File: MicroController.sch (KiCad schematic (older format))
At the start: 59 parts, among them J301 Conn_02x03_Odd_Even, Q301 IRLML0040TR, Q302 IRLML0040TR, SW301 TACTILE_SWITCHPTS540-SMD, SW302 TACTILE_SWITCHPTS540-SMD, SW303 TACTILE_SWITCHPTS540-SMD, SW304 TACTILE_SWITCHPTS540-SMD, SW305 TACTILE_SWITCHPTS540-SMD, SW306 TACTILE_SWITCHPTS540-SMD, SW307 TACTILE_SWITCHPTS540-SMD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

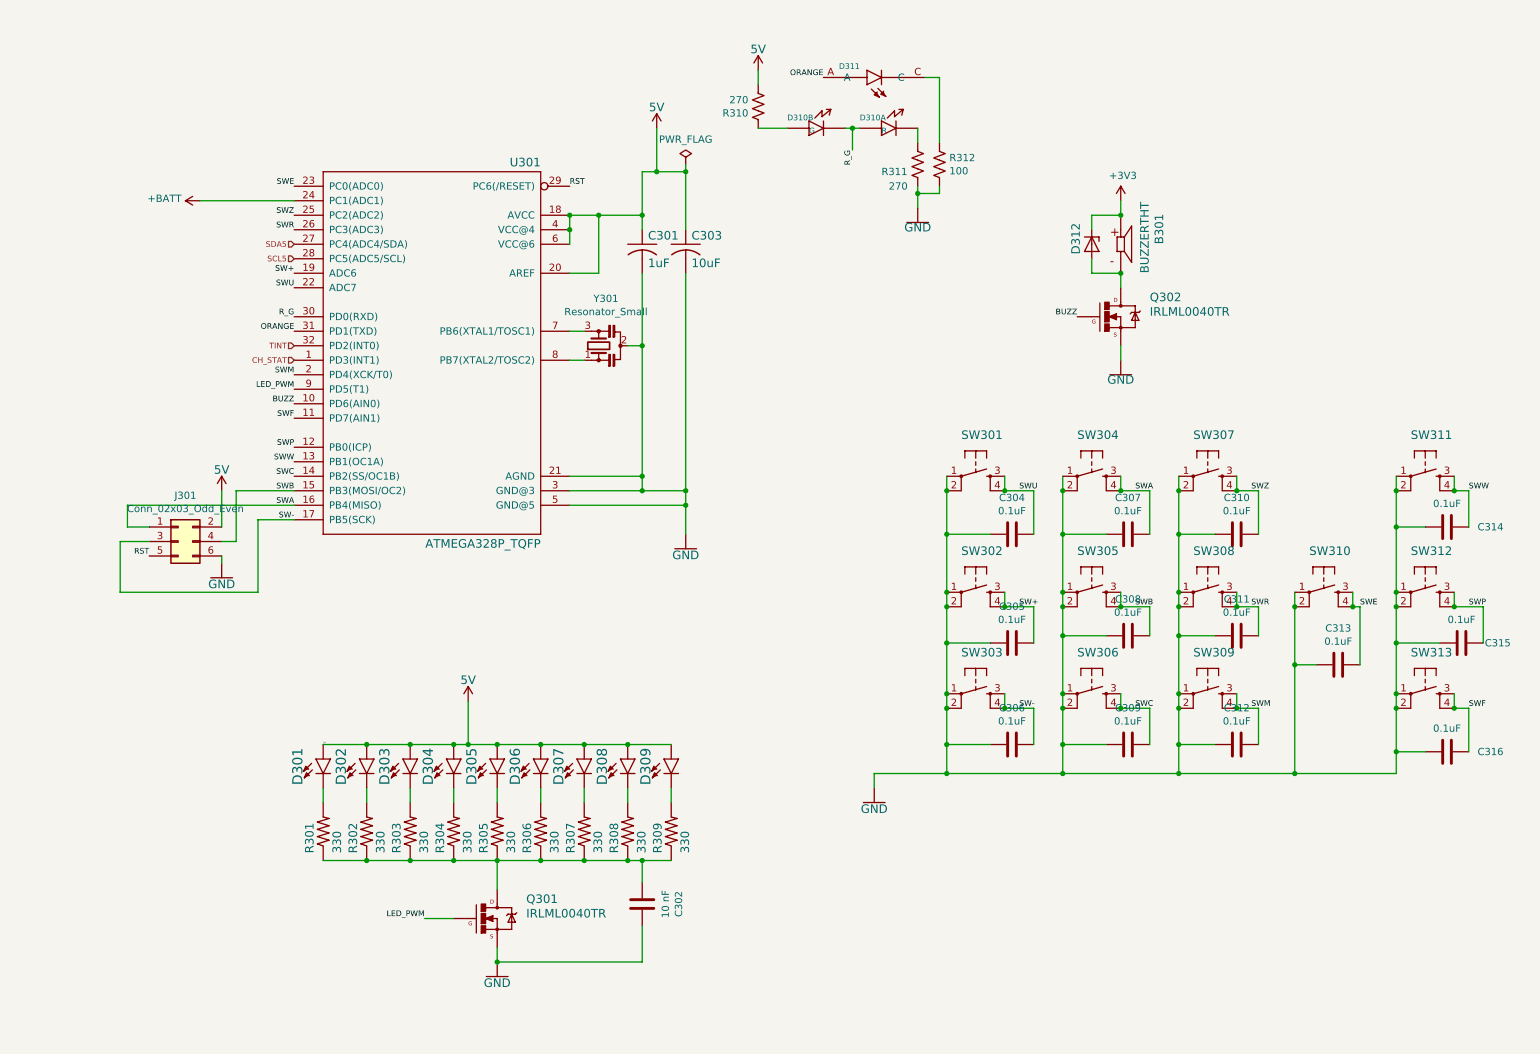
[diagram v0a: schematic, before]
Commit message: Last version before switching to resistive model to read the scroll wheel.
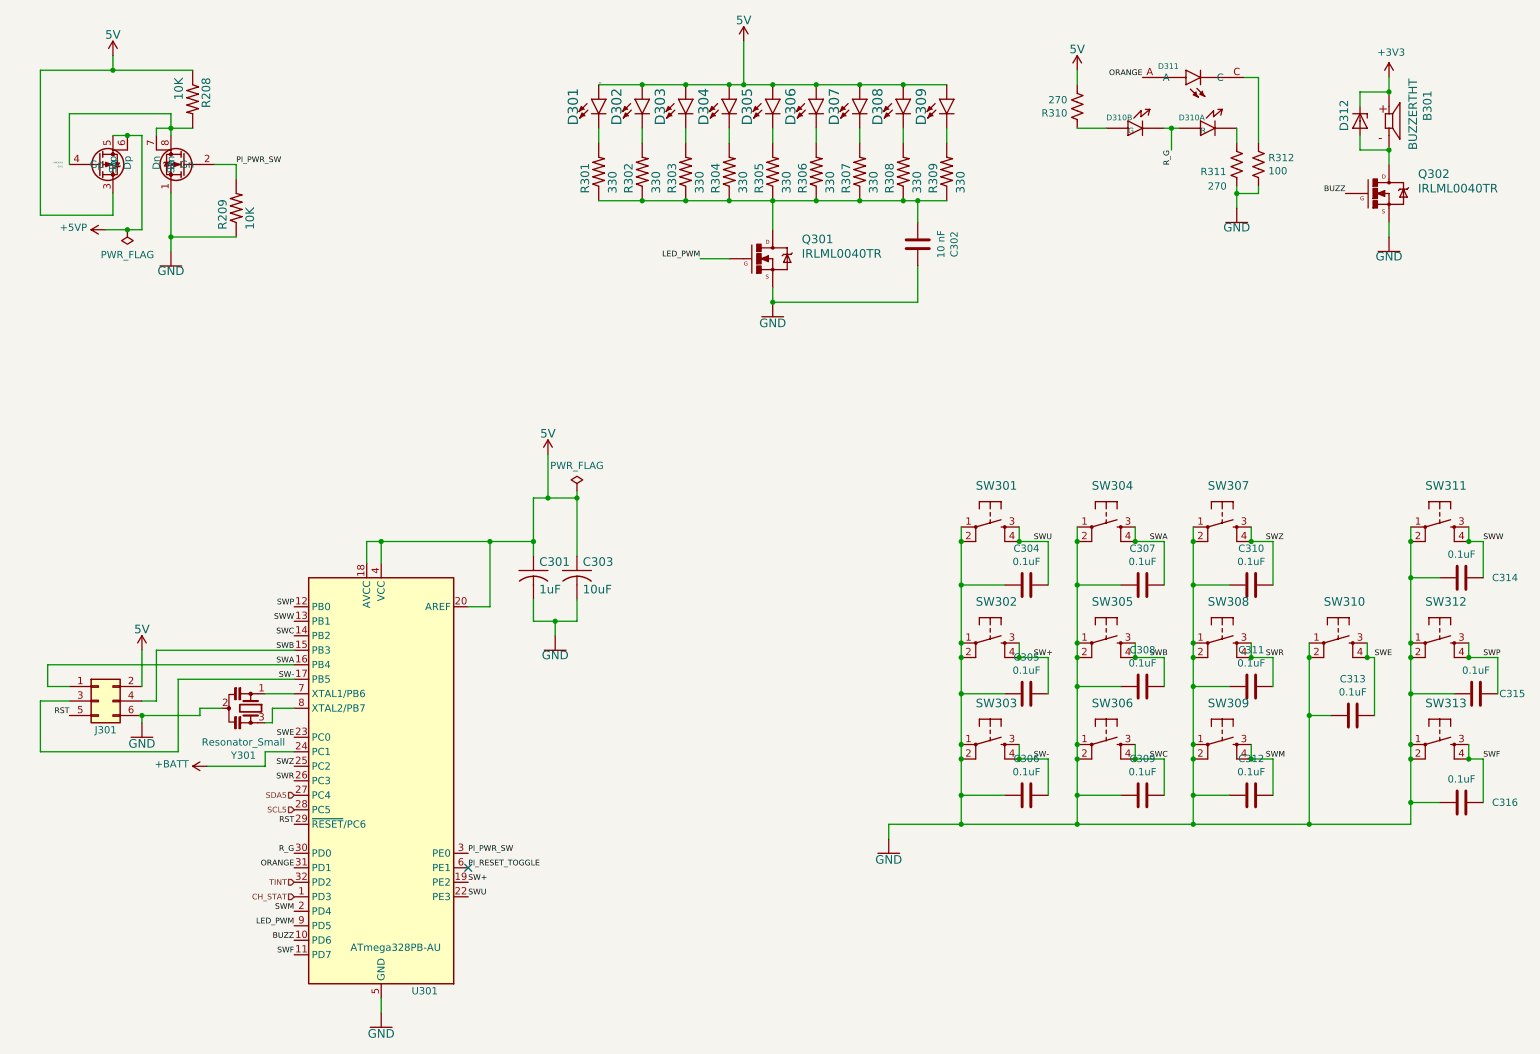
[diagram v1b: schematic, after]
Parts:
- removed U301: ATMEGA328P_TQFP, CPU:TQFP32-08, symbol CPU-eagle-import:ATMEGA328P_TQFP
- added Q201: DMC4050, Marco:8-SMD, symbol Marco:DMC4050
- added R208, R209: 10K, CPU:R1206, symbol CPU-eagle-import:R-US_R1206
- added U301: ATmega328PB-AU, Package_QFP:TQFP-32_7x7mm_P0.8mm, symbol MCU_Microchip_ATmega:ATmega328PB-AU
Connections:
- net +BATT: now also U301.24 (PC1)
- net BUZZ: now also U301.10 (PD6)
- net CH_STAT: now also U301.1 (PD3)
- net LED_PWM: now also U301.9 (PD5)
- net ORANGE: now also U301.31 (PD1)
- net RST: now also U301.29 (~RESET~/PC6)
- net R_G: now also U301.30 (PD0)
- net SCL5: now also U301.28 (PC5)
- net SDA5: now also U301.27 (PC4)
- net SW+: now also U301.19 (PE2)
- net SW-: now also U301.17 (PB5)
- net SWA: now also U301.16 (PB4)
- net SWB: now also U301.15 (PB3)
- net SWC: now also U301.14 (PB2)
- net SWE: now also U301.23 (PC0)
- net SWF: now also U301.11 (PD7)
- net SWM: now also U301.2 (PD4)
- net SWP: now also U301.12 (PB0)
- net SWR: now also U301.26 (PC3)
- net SWU: now also U301.22 (PE3)
- net SWW: now also U301.13 (PB1)
- net SWZ: now also U301.25 (PC2)
- net TINT: now also U301.32 (PD2)
- net at C301.1, C303.1: now also U301.18 (AVCC), U301.20 (AREF), U301.4 (VCC)
- net at C301.2, C303.2: no longer Y301.2
- net at Y301.3: now also U301.8 (XTAL2/PB7)
- net at Y301.1: now also U301.7 (XTAL1/PB6)
- net at J301.6 (Pin_6): now also Y301.2
- new net: U301.21 (GND), U301.5 (GND)
- new net: Q201.1 (Sn), R209.1
- new net: Q201.3 (Sp), R208.1
- new net: Q201.4 (Gp), Q201.7 (Dn), Q201.8 (Dn), R208.2
- new net +5VP: Q201.5 (Dp), Q201.6 (Dp)
- new net PI_PWR_SW: Q201.2 (Gn), R209.2, U301.3 (PE0)
- new net PI_RESET_TOGGLE: U301.6 (PE1)
- no-connect marks 0 -> 1
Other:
- moved on the sheet: B301, C302, C304, C305, C306, C307, C308, C309, C310, C311, C312, C313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

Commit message: Version 2, DRC and ERC clear, ready to send, waiting on V1 to see what did not work.
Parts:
- removed C302: 10 nF, Capacitor_SMD:C_0805_2012Metric_Pad1.15x1.40mm_HandSolder, symbol Device:C
- removed D301, D302, D303, D304, D305, D306, D307, D308, D309: LED0603, CPU:LED-0603, symbol CPU-eagle-import:LED0603
- removed D310: RG, CPU:INOLUX_IN-S85DATRG, symbol CPU-eagle-import:DUAL_LEDINOLUX
- removed D311: 598-8030-107F, CPU:LEDSC160X80X70L45N, symbol CPU-eagle-import:598-8030-107F
- removed Q301: IRLML0040TR, CPU:SOT23, symbol CPU-eagle-import:IRLML0040TR
- removed R301, R302, R303, R304, R305, R306, R307, R308, R309: 330, CPU:R1206, symbol CPU-eagle-import:R-US_R1206
- removed R310, R311: 270, Resistor_SMD:R_0805_2012Metric_Pad1.15x1.40mm_HandSolder, symbol Device:R_US
- removed R312: 100, Resistor_SMD:R_0805_2012Metric_Pad1.15x1.40mm_HandSolder, symbol Device:R_US
- removed U301: ATmega328PB-AU, Package_QFP:TQFP-32_7x7mm_P0.8mm, symbol MCU_Microchip_ATmega:ATmega328PB-AU
- added U301: ATmega328PB-AU, Package_QFP:TQFP-32_7x7mm_P0.8mm, symbol MarcoK:ATmega328PB-AU
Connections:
- net +BATT: now also U301.24 (PCI9/ADC1/Y1/SCK1/PC1)
- net BUZZ: now also U301.10 (PCI22/AIN0/X6/Y14/OC0A/PD6)
- net CH_STAT: now also U301.1 (INT1/PCI19/X3/Y11/OC2B/PD3)
- net PI_PWR_SW: now also U301.9 (PCI21/X5/Y13/OC0B/T1/PD5)
- net PI_RESET_TOGGLE: now also U301.30 (PCI16/X0/Y8/OC3A/RXD0/PD0)
- net RST: now also U301.29 (~RESET~/PCI14/PC6)
- net SCL5: now also U301.28 (PCI13/ADC5/Y5/SCL0/PC5)
- net SDA5: now also U301.27 (PCI12/ADC4/Y4/SDA0/PC4)
- net SW+: now also U301.19 (PE2/PCI26/ADC6/Y6/ICP3/~SS1~)
- net SW-: now also U301.17 (PCI5/X15/Y23/XCK1/SCK0/PB5)
- net SWA: now also U301.16 (PCI4/X14/Y22/RXD1/MISO0/PB4)
- net SWB: now also U301.15 (PCI3/X13/Y21/OC2A/TXD1/MOSI0/PB3)
- net SWC: now also U301.14 (PCI2/X12/Y20/OC1B/~SS0~/PB2)
- net SWE: now also U301.23 (PCI8/ADC0/Y0/MISO1/PC0)
- net SWF: now also U301.11 (PCI23/AIN1/X7/Y15/PD7)
- net SWM: now also U301.2 (PCI20/X4/Y12/T0/XCK0/PD4)
- net SWP: now also U301.12 (PCI/0/X10/Y18/CLKO/ICP1/PB0)
- net SWR: now also U301.26 (PCI11/ADC3/Y3/PC3)
- net SWU: now also U301.22 (PE3/PCI27/ADC7/Y7/T3/MOSI1)
- net SWW: now also U301.13 (PCI1/X11/Y19/OC1A/PB1)
- net SWZ: now also U301.25 (PCI10/ADC2/Y2/PC2)
- net at C301.1, C303.1: now also U301.18 (AVCC), U301.20 (AREF), U301.4 (VCC)
- net at Y301.1: now also U301.7 (PCI6/TOSC1/XTAL1/PB6)
- net at Y301.3: now also U301.8 (PCI7/TOSC2/XTAL2/PB7)
- new net: U301.21 (GND), U301.5 (GND)
- new net 85RES: U301.32 (INT0/PCI18/X2/Y10/OC3B/OC4B/PD2)
- new net SCROLL_INT: U301.31 (PCI17/X1/Y9/OC4A/TXD0/PD1)
- no-connect marks 1 -> 3
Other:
- note removed: "G"
- note removed: "R"
- moved on the sheet: B301, C301, C303, C304, C305, C306, C307, C308, C309, C310, C311, C312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
